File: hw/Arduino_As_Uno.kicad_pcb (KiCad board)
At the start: 2 copper layers, 68.6 x 53.3 mm, 70 parts, among them CON1 BARREL_JACK, P1 USB_OTG, P10 CONN_01X06, P11 CONN_01X08, P13 CONN_02X03, P14 CONN_02X03_ICSP, P15 CONN_01X08, P2 CONN_02X03_ICSP, P22 CONN_02X03_ICSP, P3 CONN_02X03, P4 CONN_02X03_ICSP, P5 CONN_01X08, P6 CONN_02X03, P7 CONN_02X03_ICSP, P8 CONN_02X03_ICSP, P9 CONN_01X10, Q1 FDN340P, SW1 SW_PUSH, U1 LM2940LD-5.0, U10 TS3A44159, U11 FDG6331L, U2 MIC5205, U3 ATMEGA16U2, U4 23K256, U5 ATTINY85-SUR, U6 TS3A44159, U7 ATMEGA328PB-MU, U8 74LVCH1T45, U9 ATTINY85-SUR, X1 CRYSTAL, X2 RESONATOR

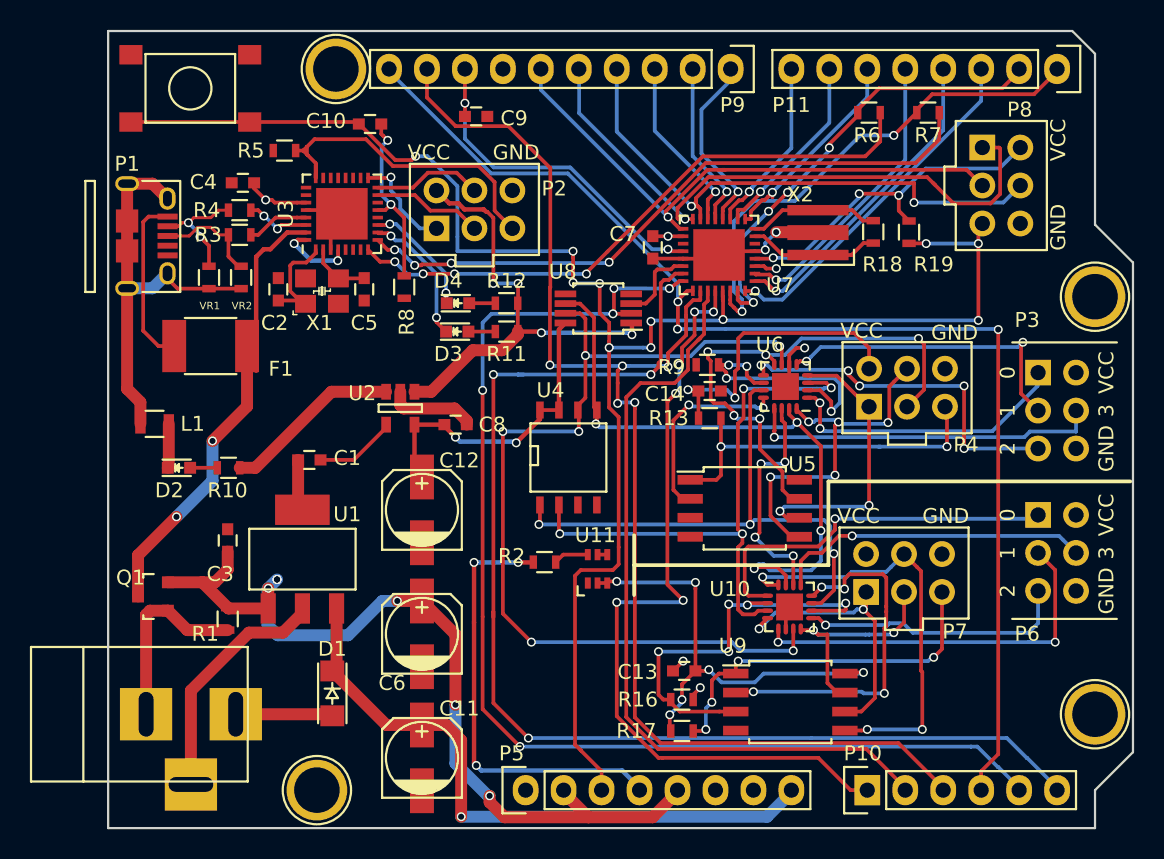
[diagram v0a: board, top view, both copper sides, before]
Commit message: add ground plane and stitching vias. All signals routed.
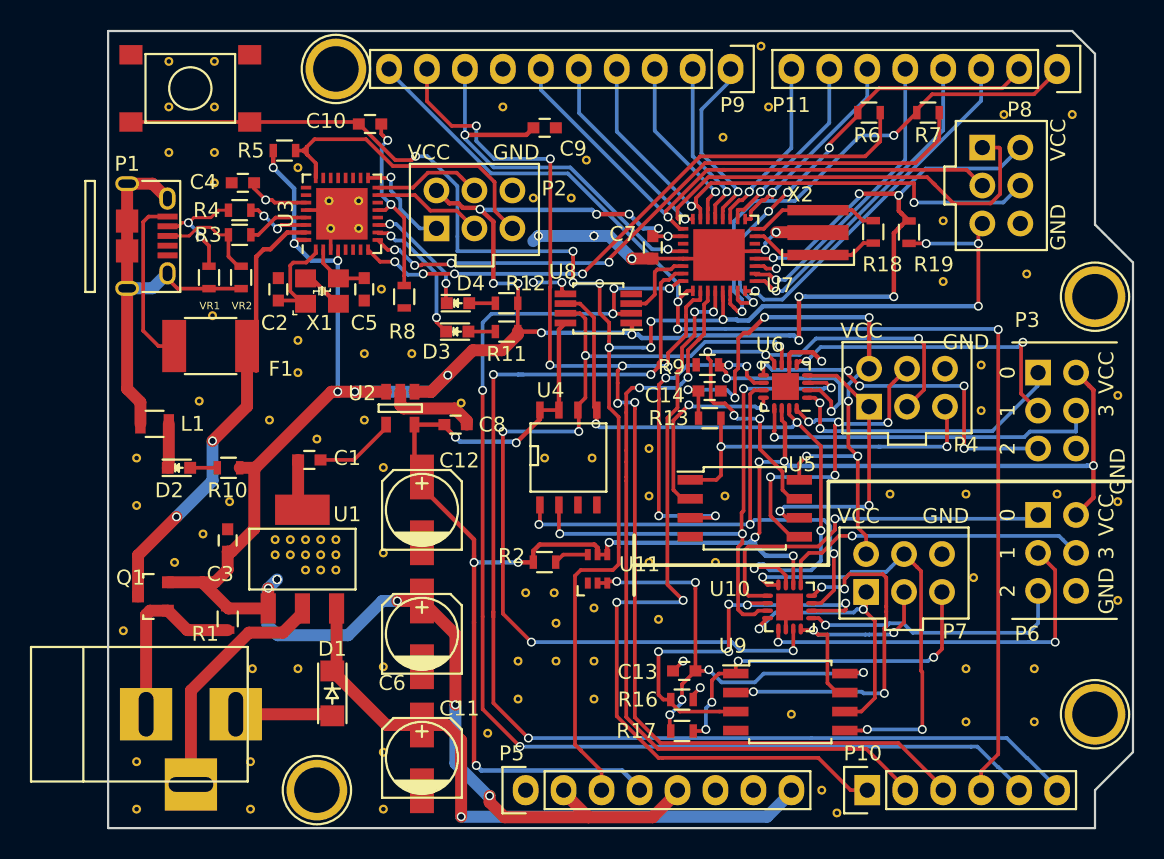
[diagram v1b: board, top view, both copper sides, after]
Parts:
- added REF**: stitchingVIA, pcbfp_lib:via_.3, F.Cu at (156.7, 118.7)
- added REF**: stitchingVIA, pcbfp_lib:via_.3, F.Cu at (125.8, 84.4)
- added REF**: stitchingVIA, pcbfp_lib:via_.3, F.Cu at (126.2, 107.1)
- added REF**: stitchingVIA, pcbfp_lib:via_.3, F.Cu at (124.2, 107.1)
- added REF**: stitchingVIA, pcbfp_lib:via_.3, F.Cu at (123.2, 107.1)
- added REF**: stitchingVIA, pcbfp_lib:via_.3, F.Cu at (122.2, 107.1)
- added REF**: stitchingVIA, pcbfp_lib:via_.3, F.Cu at (125.2, 107.1)
- added REF**: stitchingVIA, pcbfp_lib:via_.3, F.Cu at (123.2, 108.1)
- added REF**: stitchingVIA, pcbfp_lib:via_.3, F.Cu at (124.2, 109.1)
- added REF**: stitchingVIA, pcbfp_lib:via_.3, F.Cu at (124.2, 108.1)
- added REF**: stitchingVIA, pcbfp_lib:via_.3, F.Cu at (125.2, 108.1)
- added REF**: stitchingVIA, pcbfp_lib:via_.3, F.Cu at (168.4, 119.3)
- added REF**: stitchingVIA, pcbfp_lib:via_.3, F.Cu at (125.2, 109.1)
- added REF**: stitchingVIA, pcbfp_lib:via_.3, F.Cu at (126.2, 109.1)
- added REF**: stitchingVIA, pcbfp_lib:via_.3, F.Cu at (137.4, 78.1)
- added REF**: stitchingVIA, pcbfp_lib:via_.3, F.Cu at (143.0, 81.7)
- added REF**: stitchingVIA, pcbfp_lib:via_.3, F.Cu at (139.4, 84.2)
- added REF**: stitchingVIA, pcbfp_lib:via_.3, F.Cu at (142.0, 84.2)
- added REF**: stitchingVIA, pcbfp_lib:via_.3, F.Cu at (174.5, 104.0)
- added REF**: stitchingVIA, pcbfp_lib:via_.3, F.Cu at (173.0, 115.7)
- added REF**: stitchingVIA, pcbfp_lib:via_.3, F.Cu at (173.0, 119.3)
- added REF**: stitchingVIA, pcbfp_lib:via_.3, F.Cu at (159.8, 125.3)
- added REF**: stitchingVIA, pcbfp_lib:via_.3, F.Cu at (168.4, 115.7)
- added REF**: stitchingVIA, pcbfp_lib:via_.3, F.Cu at (158.8, 123.8)
- added REF**: stitchingVIA, pcbfp_lib:via_.3, F.Cu at (143.5, 117.7)
- added REF**: stitchingVIA, pcbfp_lib:via_.3, F.Cu at (143.5, 115.2)
- added REF**: stitchingVIA, pcbfp_lib:via_.3, F.Cu at (143.5, 111.6)
- added REF**: stitchingVIA, pcbfp_lib:via_.3, F.Cu at (123.7, 115.7)
- added REF**: stitchingVIA, pcbfp_lib:via_.3, F.Cu at (120.7, 115.7)
- added REF**: stitchingVIA, pcbfp_lib:via_.3, F.Cu at (112.0, 113.2)
- added REF**: stitchingVIA, pcbfp_lib:via_.3, F.Cu at (119.1, 104.5)
- added REF**: stitchingVIA, pcbfp_lib:via_.3, F.Cu at (118.1, 83.2)
- added REF**: stitchingVIA, pcbfp_lib:via_.3, F.Cu at (115.1, 81.2)
- added REF**: stitchingVIA, pcbfp_lib:via_.3, F.Cu at (168.9, 109.6)
- added REF**: stitchingVIA, pcbfp_lib:via_.3, F.Cu at (118.1, 81.2)
- added REF**: stitchingVIA, pcbfp_lib:via_.3, F.Cu at (118.1, 78.1)
- added REF**: stitchingVIA, pcbfp_lib:via_.3, F.Cu at (115.1, 78.1)
- added REF**: stitchingVIA, pcbfp_lib:via_.3, F.Cu at (118.1, 75.1)
- added REF**: stitchingVIA, pcbfp_lib:via_.3, F.Cu at (115.1, 75.1)
- added REF**: stitchingVIA, pcbfp_lib:via_.3, F.Cu at (154.7, 74.0)
- added REF**: stitchingVIA, pcbfp_lib:via_.3, F.Cu at (155.2, 78.1)
- added REF**: stitchingVIA, pcbfp_lib:via_.3, F.Cu at (152.1, 80.1)
- added REF**: stitchingVIA, pcbfp_lib:via_.3, F.Cu at (178.6, 111.1)
- added REF**: stitchingVIA, pcbfp_lib:via_.3, F.Cu at (178.6, 104.5)
- added REF**: stitchingVIA, pcbfp_lib:via_.3, F.Cu at (123.7, 82.2)
- added REF**: stitchingVIA, pcbfp_lib:via_.3, F.Cu at (178.6, 97.4)
- added REF**: stitchingVIA, pcbfp_lib:via_.3, F.Cu at (169.4, 98.4)
- added REF**: stitchingVIA, pcbfp_lib:via_.3, F.Cu at (169.4, 95.4)
- added REF**: stitchingVIA, pcbfp_lib:via_.3, F.Cu at (166.9, 89.8)
- added REF**: stitchingVIA, pcbfp_lib:via_.3, F.Cu at (166.9, 85.7)
- added REF**: stitchingVIA, pcbfp_lib:via_.3, F.Cu at (170.9, 78.6)
- added REF**: stitchingVIA, pcbfp_lib:via_.3, F.Cu at (175.5, 78.6)
- added REF**: stitchingVIA, pcbfp_lib:via_.3, F.Cu at (172.5, 89.3)
- added REF**: stitchingVIA, pcbfp_lib:via_.3, F.Cu at (168.4, 104.0)
- added REF**: stitchingVIA, pcbfp_lib:via_.3, F.Cu at (163.3, 104.0)
- added REF**: stitchingVIA, pcbfp_lib:via_.3, F.Cu at (129.3, 90.3)
- added REF**: stitchingVIA, pcbfp_lib:via_.3, F.Cu at (152.3, 104.1)
- added REF**: stitchingVIA, pcbfp_lib:via_.3, F.Cu at (151.6, 108.6)
- added REF**: stitchingVIA, pcbfp_lib:via_.3, F.Cu at (147.8, 112.4)
- added REF**: stitchingVIA, pcbfp_lib:via_.3, F.Cu at (147.2, 108.6)
- added REF**: stitchingVIA, pcbfp_lib:via_.3, F.Cu at (147.2, 104.1)
- added REF**: stitchingVIA, pcbfp_lib:via_.3, F.Cu at (147.2, 101.0)
- added REF**: stitchingVIA, pcbfp_lib:via_.3, F.Cu at (143.4, 101.6)
- added REF**: stitchingVIA, pcbfp_lib:via_.3, F.Cu at (140.2, 101.6)
- added REF**: stitchingVIA, pcbfp_lib:via_.3, F.Cu at (138.9, 110.6)
- added REF**: stitchingVIA, pcbfp_lib:via_.3, F.Cu at (141.0, 112.6)
- added REF**: stitchingVIA, pcbfp_lib:via_.3, F.Cu at (125.9, 86.2)
- added REF**: stitchingVIA, pcbfp_lib:via_.3, F.Cu at (140.8, 110.6)
- added REF**: stitchingVIA, pcbfp_lib:via_.3, F.Cu at (141.0, 115.2)
- added REF**: stitchingVIA, pcbfp_lib:via_.3, F.Cu at (138.4, 115.2)
- added REF**: stitchingVIA, pcbfp_lib:via_.3, F.Cu at (138.4, 117.7)
- added REF**: stitchingVIA, pcbfp_lib:via_.3, F.Cu at (136.4, 120.0)
- added REF**: stitchingVIA, pcbfp_lib:via_.3, F.Cu at (129.4, 121.3)
- added REF**: stitchingVIA, pcbfp_lib:via_.3, F.Cu at (129.4, 125.1)
- added REF**: stitchingVIA, pcbfp_lib:via_.3, F.Cu at (129.4, 115.6)
- added REF**: stitchingVIA, pcbfp_lib:via_.3, F.Cu at (129.4, 108.0)
- added REF**: stitchingVIA, pcbfp_lib:via_.3, F.Cu at (129.4, 102.2)
- added REF**: stitchingVIA, pcbfp_lib:via_.3, F.Cu at (127.8, 86.2)
- added REF**: stitchingVIA, pcbfp_lib:via_.3, F.Cu at (112.9, 125.1)
- added REF**: stitchingVIA, pcbfp_lib:via_.3, F.Cu at (112.9, 121.9)
- added REF**: stitchingVIA, pcbfp_lib:via_.3, F.Cu at (120.5, 125.1)
- added REF**: stitchingVIA, pcbfp_lib:via_.3, F.Cu at (120.5, 121.9)
- added REF**: stitchingVIA, pcbfp_lib:via_.3, F.Cu at (122.2, 108.1)
- added REF**: stitchingVIA, pcbfp_lib:via_.3, F.Cu at (126.2, 108.1)
- added REF**: stitchingVIA, pcbfp_lib:via_.3, F.Cu at (115.4, 108.6)
- added REF**: stitchingVIA, pcbfp_lib:via_.3, F.Cu at (117.3, 106.7)
- added REF**: stitchingVIA, pcbfp_lib:via_.3, F.Cu at (112.9, 101.6)
- added REF**: stitchingVIA, pcbfp_lib:via_.3, F.Cu at (112.9, 104.8)
- added REF**: stitchingVIA, pcbfp_lib:via_.3, F.Cu at (127.8, 84.4)
- added REF**: stitchingVIA, pcbfp_lib:via_.3, F.Cu at (118.0, 92.1)
- added REF**: stitchingVIA, pcbfp_lib:via_.3, F.Cu at (125.0, 100.3)
- added REF**: stitchingVIA, pcbfp_lib:via_.3, F.Cu at (128.1, 99.1)
- added REF**: stitchingVIA, pcbfp_lib:via_.3, F.Cu at (117.1, 97.8)
- added REF**: stitchingVIA, pcbfp_lib:via_.3, F.Cu at (121.8, 99.1)
- added REF**: stitchingVIA, pcbfp_lib:via_.3, F.Cu at (123.7, 95.9)
- added REF**: stitchingVIA, pcbfp_lib:via_.3, F.Cu at (131.3, 94.6)
- added REF**: stitchingVIA, pcbfp_lib:via_.3, F.Cu at (128.1, 94.6)
- added REF**: stitchingVIA, pcbfp_lib:via_.3, F.Cu at (123.7, 93.7)
- added REF**: stitchingVIA, pcbfp_lib:via_.3, F.Cu at (134.6, 97.9)
- moved C9 4.65 mm to (140.2, 79.5)
- moved R8 0.65 mm to (130.8, 90.8)
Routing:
- net +5V: track 132.3 -> 200.5 mm, vias 16 -> 27
- net +3V3: track 67.5 -> 122.7 mm, vias 9 -> 11
- net /3.3V_UNSAFE: track 51.6 -> 73.9 mm, vias 8 -> 13
- net /SELECT_T1: track 17.4 -> 36.9 mm, vias 4 -> 7
- net GND: track 54.2 -> 70.0 mm, vias 5 -> 10
- net /AREF: track 23.3 -> 27.3 mm
- net /AD2/SDA: track 87.2 -> 88.3 mm, vias 5 -> 7
- net Net-(C10-Pad2): track 12.2 -> 12.8 mm
- net /AD1: track 53.1 -> 53.6 mm, vias 0 -> 2
- net /AD0: track 54.3 -> 54.2 mm, vias 6 -> 4
- added copper zone on B.Cu, net GND
- added copper zone on F.Cu, net GND

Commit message: End of day commit. 12 Unconnected nets. Needs some silikscreen.
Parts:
- added REF**: stitchingVIA, pcbfp_lib:via_.3, F.Cu at (146.3, 121.8)
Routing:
- net GND: track 70.0 -> 76.8 mm, vias 10 -> 12
- net /SCK_T1: track 35.0 -> 35.6 mm
- net /AD4/SCK1: vias 5 -> 4
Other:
- board text added: "Paul Ugolino"
- board text added: "T1"
- board text added: "T2"
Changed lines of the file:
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@@
   (general
     (links 338)
-    (no_connects 10)
+    (no_connects 7)
     (area 110.922999 72.949999 179.653001 126.440001)
     (thickness 1.6)
-    (drawings 19)
-    (tracks 1523)
+    (drawings 22)
+    (tracks 1534)
     (zones 0)
-    (modules 169)
+    (modules 170)
     (nets 100)
   )
@@
   )
   (module pcbfp_lib:via_.3 (layer F.Cu)
+    (at 146.304 121.793)
+    (fp_text reference REF** (at 0 1.524) (layer F.SilkS) hide
+      (effects (font (size 1 1) (thickness 0.15)))
+    )
+    (fp_text value stitchingVIA (at 0 -1.27) (layer F.Fab) hide
+      (effects (font (size 1 1) (thickness 0.15)))
+    )
+    (pad 1 thru_hole circle (at 0 0) (size 0.6 0.6) (drill 0.3) (layers *.Cu *.Mask)
+      (net 2 GND) (zone_connect 2))
+  )
+  (module pcbfp_lib:via_.3 (layer F.Cu)
     (at 156.718 118.745)
     (fp_text reference REF** (at 0 1.524) (layer F.SilkS) hide
@@
     (tags "resistor 0603")
     (attr smd)
-    (fp_text reference R2 (at -2.2 -0.4) (layer F.SilkS)
+    (fp_text reference R2 (at -2.2 -1.25) (layer F.SilkS)
       (effects (font (size 1 1) (thickness 0.15)))
     )
@@
     (tags "capacitor 0603")
     (attr smd)
-    (fp_text reference C8 (at 2.45 0) (layer F.SilkS)
+    (fp_text reference C8 (at 2.45 -0.432) (layer F.SilkS)
       (effects (font (size 1 1) (thickness 0.15)))
     )
@@
     (tags "SOIC 1.27")
     (attr smd)
-    (fp_text reference U9 (at -3.85 -3.765 180) (layer F.SilkS)
+    (fp_text reference U9 (at -2.216 -3.757 180) (layer F.SilkS)
       (effects (font (size 1 1) (thickness 0.15)))
     )
@@
       (effects (font (size 1 1) (thickness 0.15)))
     )
-    (fp_text user GND (at 5.334 6.604 90) (layer F.SilkS)
+    (fp_text user GND (at 4.572 5.334 90) (layer F.SilkS)
       (effects (font (size 1 1) (thickness 0.15)))
     )
@@
     (tags SC-70-6,)
     (attr smd)
-    (fp_text reference U11 (at 2.81024 -0.30304) (layer F.SilkS)
+    (fp_text reference U11 (at -0.23776 3.63396) (layer F.SilkS)
       (effects (font (size 1 1) (thickness 0.15)))
     )
@@
       (net 2 GND) (zone_connect 2))
   )
+  (gr_text T2 (at 164.592 101.981) (layer F.SilkS)
+    (effects (font (size 1.5 1.5) (thickness 0.3)))
+  )
+  (gr_text T1 (at 164.338 114.935) (layer F.SilkS)
+    (effects (font (size 1.5 1.5) (thickness 0.3)))
+  )
+  (gr_text "Paul Ugolino\n\n\n" (at 130.302 106.045) (layer B.SilkS)
+    (effects (font (size 1.5 1.5) (thickness 0.3)) (justify mirror))
+  )
   (gr_line (start 146.198 106.765) (end 146.198 110.765) (layer F.SilkS) (width 0.25))
   (gr_line (start 159.198 103.165) (end 179.398 103.165) (layer F.SilkS) (width 0.25))
@@
   (segment (start 114.99876 109.915) (end 117.298 109.915) (width 0.8) (layer F.Cu) (net 1))
   (segment (start 117.298 109.915) (end 118.998 111.615) (width 0.8) (layer F.Cu) (net 1))
+  (segment (start 146.05 88.265) (end 146.05 90.563) (width 0.25) (layer F.Cu) (net 2))
+  (segment (start 146.05 90.563) (end 145.998 90.615) (width 0.25) (layer F.Cu) (net 2))
+  (segment (start 151.998 97.115) (end 151.998 97.74) (width 0.25) (layer F.Cu) (net 2))
+  (via (at 152.908 100.203) (size 0.6) (drill 0.4) (layers F.Cu B.Cu) (net 2))
+  (segment (start 151.998 97.74) (end 152.908 98.65) (width 0.25) (layer F.Cu) (net 2))
+  (segment (start 152.908 98.65) (end 152.908 100.203) (width 0.25) (layer F.Cu) (net 2))
+  (segment (start 150.348 95.365) (end 150.348 95.739011) (width 0.25) (layer F.Cu) (net 2))
+  (segment (start 150.348 95.739011) (end 150.747989 96.139) (width 0.25) (layer F.Cu) (net 2))
+  (via (at 150.747989 96.139) (size 0.6) (drill 0.4) (layers F.Cu B.Cu) (net 2))
   (segment (start 141.362804 89.847646) (end 139.446 89.847646) (width 0.25) (layer B.Cu) (net 2))
   (via (at 139.446 89.847646) (size 0.6) (drill 0.4) (layers F.Cu B.Cu) (net 2))
@@
   (segment (start 126.284 111.667) (end 126.284 115.562) (width 0.8) (layer F.Cu) (net 11))
   (segment (start 126.284 115.562) (end 125.998 115.848) (width 0.8) (layer F.Cu) (net 11))
+  (segment (start 152.908 97.409) (end 152.908 96.576994) (width 0.25) (layer F.Cu) (net 12))
+  (segment (start 152.908 96.576994) (end 152.942993 96.542001) (width 0.25) (layer F.Cu) (net 12))
+  (segment (start 152.942993 96.542001) (end 152.942993 95.812009) (width 0.25) (layer F.Cu) (net 12))
+  (segment (start 152.396969 97.028) (end 152.527 97.028) (width 0.25) (layer B.Cu) (net 12))
+  (segment (start 152.527 97.028) (end 152.908 97.409) (width 0.25) (layer B.Cu) (net 12))
+  (via (at 152.908 97.409) (size 0.6) (drill 0.4) (layers F.Cu B.Cu) (net 12))
   (segment (start 161.925 92.202) (end 161.925 95.618) (width 0.3) (layer F.Cu) (net 12))
   (segment (start 161.925 95.618) (end 161.918 95.625) (width 0.3) (layer F.Cu) (net 12))
@@
   (segment (start 149.80002 97.06702) (end 149.80002 97.028) (width 0.25) (layer F.Cu) (net 12))
   (segment (start 150.498 97.115) (end 149.848 97.115) (width 0.25) (layer F.Cu) (net 12))
-  (segment (start 152.943002 97.574033) (end 152.396969 97.028) (width 0.25) (layer B.Cu) (net 12))
-  (segment (start 152.943002 97.574033) (end 152.943002 95.812) (width 0.25) (layer F.Cu) (net 12))
   (segment (start 153.162 95.593002) (end 153.162 93.599) (width 0.25) (layer F.Cu) (net 12))
   (segment (start 152.943002 95.812) (end 153.162 95.593002) (width 0.25) (layer F.Cu) (net 12))
   (segment (start 153.162 93.599) (end 153.52399 93.23701) (width 0.25) (layer F.Cu) (net 12))
   (segment (start 161.918 94.227) (end 161.918 95.625) (width 0.25) (layer F.Cu) (net 12))
-  (via (at 152.943002 97.574033) (size 0.6) (drill 0.4) (layers F.Cu B.Cu) (net 12))
   (segment (start 150.298 109.925) (end 150.298 110.349264) (width 0.25) (layer F.Cu) (net 12))
   (segment (start 150.298 110.349264) (end 150.298 115.846) (width 0.25) (layer F.Cu) (net 12))
@@
   (segment (start 156.4 105.6) (end 155.956 105.156) (width 0.25) (layer F.Cu) (net 33))
   (via (at 155.956 105.156) (size 0.6) (drill 0.4) (layers F.Cu B.Cu) (net 33))
+  (segment (start 151.306998 98.871999) (end 153.002477 98.871999) (width 0.25) (layer B.Cu) (net 34))
+  (segment (start 153.002477 98.871999) (end 153.097007 98.966529) (width 0.25) (layer B.Cu) (net 34))
+  (segment (start 151.322999 98.708043) (end 151.306998 98.871999) (width 0.25) (layer F.Cu) (net 34))
+  (segment (start 151.322999 98.871999) (end 151.306998 98.871999) (width 0.25) (layer F.Cu) (net 34))
+  (via (at 151.306998 98.871999) (size 0.6) (drill 0.4) (layers F.Cu B.Cu) (net 34))
+  (segment (start 151.322999 97.710001) (end 151.322999 98.708043) (width 0.25) (layer F.Cu) (net 34))
   (segment (start 155.00776 94.699513) (end 157.268487 94.699513) (width 0.25) (layer B.Cu) (net 34))
   (segment (start 157.268487 94.699513) (end 158.369 93.599) (width 0.25) (layer B.Cu) (net 34))
   (segment (start 158.369 93.599) (end 165.227 93.599) (width 0.25) (layer B.Cu) (net 34))
-  (segment (start 152.877646 98.747168) (end 152.877646 98.544648) (width 0.25) (layer F.Cu) (net 34))
-  (segment (start 152.877646 98.544648) (end 152.273 97.940002) (width 0.25) (layer F.Cu) (net 34))
   (segment (start 154.610275 98.966529) (end 153.097007 98.966529) (width 0.25) (layer B.Cu) (net 34))
-  (segment (start 153.097007 98.966529) (end 152.877646 98.747168) (width 0.25) (layer B.Cu) (net 34))
-  (via (at 152.877646 98.747168) (size 0.6) (drill 0.4) (layers F.Cu B.Cu) (net 34))
   (segment (start 154.610275 101.002275) (end 154.610275 99.390793) (width 0.25) (layer F.Cu) (net 34))
   (segment (start 156.122999 103.729999) (end 156.122999 102.514999) (width 0.25) (layer F.Cu) (net 34))
@@
   (segment (start 151.13 94.912264) (end 151.322999 95.105263) (width 0.25) (layer F.Cu) (net 34))
   (segment (start 151.322999 95.105263) (end 151.322999 97.710001) (width 0.25) (layer F.Cu) (net 34))
-  (segment (start 151.322999 97.710001) (end 151.553 97.940002) (width 0.25) (layer F.Cu) (net 34))
-  (segment (start 151.553 97.940002) (end 152.273 97.940002) (width 0.25) (layer F.Cu) (net 34))
   (via (at 151.13 94.488) (size 0.6) (drill 0.4) (layers F.Cu B.Cu) (net 34))
   (segment (start 159.734001 99.052989) (end 159.868012 99.187) (width 0.25) (layer B.Cu) (net 35))
@@
   (segment (start 151.126 90.41) (end 151.126 91.075698) (width 0.25) (layer F.Cu) (net 48))
   (segment (start 151.126 91.075698) (end 150.876 91.325698) (width 0.25) (layer F.Cu) (net 48))
-  (segment (start 144.845787 90.248612) (end 144.845787 91.882213) (width 0.25) (layer F.Cu) (net 49))
-  (segment (start 144.845787 91.882213) (end 144.78 91.948) (width 0.25) (layer F.Cu) (net 49))
+  (segment (start 144.858612 90.248612) (end 144.78 90.327224) (width 0.25) (layer B.Cu) (net 49))
+  (segment (start 144.78 90.327224) (end 144.78 91.948) (width 0.25) (layer B.Cu) (net 49))
+  (via (at 144.78 91.948) (size 0.6) (drill 0.4) (layers F.Cu B.Cu) (net 49))
   (segment (start 147.889055 90.254955) (end 144.845787 90.248612) (width 0.25) (layer B.Cu) (net 49))
   (segment (start 144.864955 90.254955) (end 144.858612 90.248612) (width 0.25) (layer B.Cu) (net 49))
   (segment (start 144.858612 90.248612) (end 144.845787 90.248612) (width 0.25) (layer B.Cu) (net 49))
-  (via (at 144.845787 90.248612) (size 0.6) (drill 0.4) (layers F.Cu B.Cu) (net 49))
   (segment (start 148.551675 90.254955) (end 147.889055 90.254955) (width 0.25) (layer B.Cu) (net 49))
   (segment (start 148.551675 90.254955) (end 149.251 89.76) (width 0.25) (layer F.Cu) (net 49))
@@
   (segment (start 144.78 91.948) (end 145.965 91.948) (width 0.25) (layer F.Cu) (net 49))
   (segment (start 145.965 91.948) (end 145.998 91.915) (width 0.25) (layer F.Cu) (net 49))
-  (via (at 144.78 91.948) (size 0.6) (drill 0.4) (layers F.Cu B.Cu) (net 49))
   (via (at 136.058011 97.069011) (size 0.6) (drill 0.4) (layers F.Cu B.Cu) (net 49))
   (segment (start 171.958 123.825) (end 171.831 123.825) (width 0.25) (layer F.Cu) (net 49))
